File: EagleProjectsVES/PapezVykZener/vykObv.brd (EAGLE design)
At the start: 160 x 100 mm, 19 parts, among them P1 VCC, P2 GND, P3 B, P4 C, P5 E, P6 X4, P7 X3

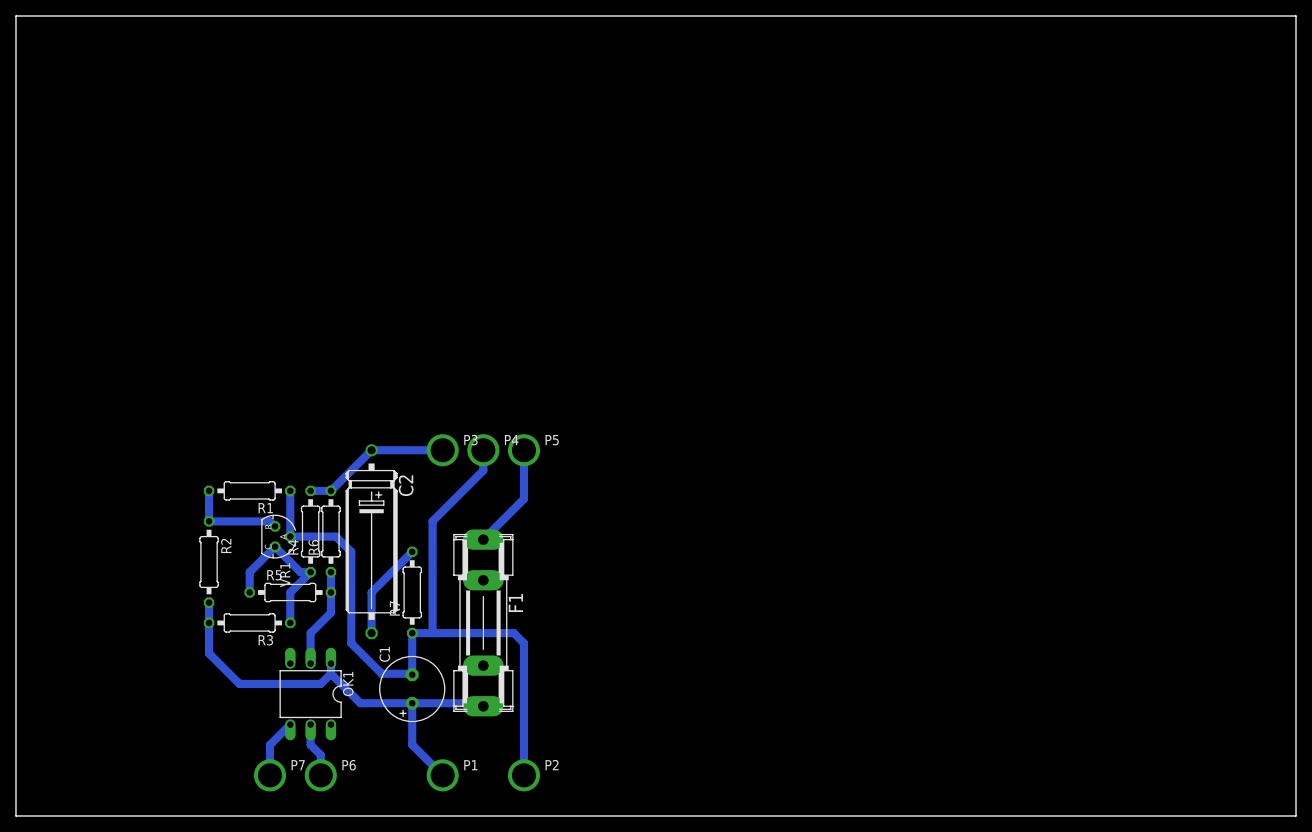
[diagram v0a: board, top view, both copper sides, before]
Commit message: Hotovy vykonovy obvod simulujici zenerovu doidu
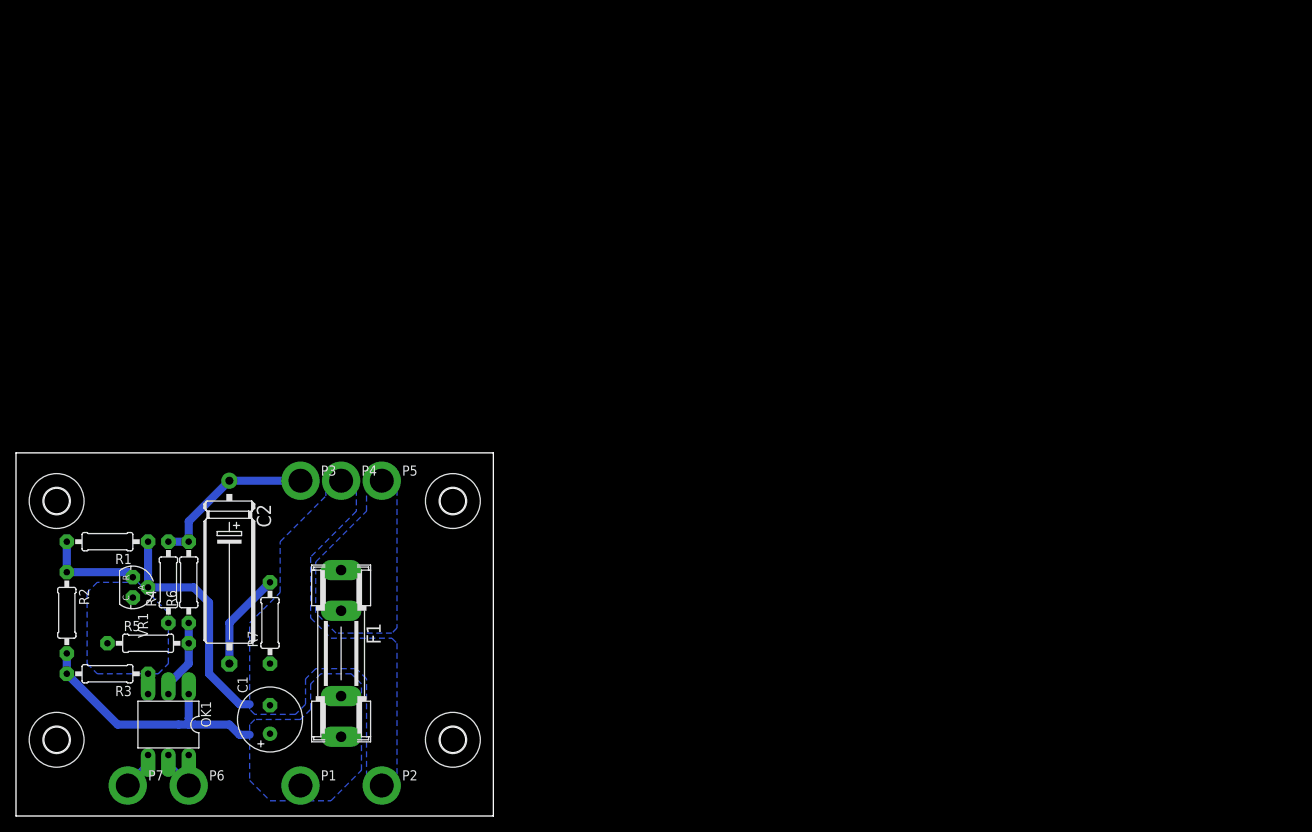
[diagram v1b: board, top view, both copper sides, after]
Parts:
- added U$1, U$2, U$3, U$4: (no value), holes:3,2
- moved R1 18.9 mm to (11.4, 34.3)
- moved R2 18.9 mm to (6.35, 25.4)
- moved R3 18.9 mm to (11.4, 17.8)
- moved R4 18.9 mm to (19.1, 29.2)
- moved R5 18.9 mm to (16.5, 21.6)
- moved R6 18.9 mm to (21.6, 29.2)
- moved VR1 18.9 mm to (14.6, 28.6)
- moved C1 18.2 mm to (31.8, 12.1)
- moved C2 18.2 mm to (26.7, 30.5)
- moved F1 18.2 mm to (40.6, 20.3)
- moved P3 18.2 mm to (35.6, 41.9)
- moved P4 18.2 mm to (40.6, 41.9)
- moved P5 18.2 mm to (45.7, 41.9)
- moved R7 18.2 mm to (31.8, 24.1)
- moved OK1 18.2 mm to (19.1, 11.4)
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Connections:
- net N$2 renamed GND
- removed net N$1: C1.+, F1.2A, OK1.1, P1.1, R2.2, R3.2
- removed net N$3: F1.1A, P5.1
- new net EMIT: F1.1A, F1.1B, P5.1
- new net VDD: C1.+, F1.2A, F1.2B, OK1.1, P1.1, R2.2, R3.2
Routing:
- net GND: track 96.5 -> 29.9 mm
- net N$1: track 56.3 -> 0.00 mm
- net VDD: track 0.00 -> 32.4 mm
- net N$7: track 20.2 -> 0.00 mm
- net N$3: track 13.3 -> 0.00 mm
- net N$5: track 12.5 -> 9.94 mm
- net N$8: track 7.40 -> 4.86 mm
- net N$6: track 18.6 -> 21.2 mm
- net N$9: track 6.88 -> 4.86 mm
- added copper zone on layer 16, net EMIT
- added copper zone on layer 16, net GND
- added copper zone on layer 16, net N$7
- added copper zone on layer 16, net VDD
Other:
- board size 160 x 100 mm -> 59.7 x 45.4 mm

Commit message: Zacatek prace na prednasce P7 pro anglicany
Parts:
- P6, P7: device PADs:PAD3MM -> PADs:PAD1.6MM
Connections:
- net N$8: now also P7.P$1; no longer P7.1
- net N$9: now also P6.P$1; no longer P6.1
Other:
- board text added: "B"
- board text added: "C"
- board text added: "E"
- board text added: "GND"
- board text added: "spodní vrstva"
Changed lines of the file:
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@@
 <grid distance="0.05" unitdist="inch" unit="inch" style="lines" multiple="1" display="yes" altdistance="0.025" altunitdist="inch" altunit="inch"/>
 <layers>
-<layer number="1" name="Top" color="4" fill="1" visible="yes" active="yes"/>
+<layer number="1" name="Top" color="4" fill="1" visible="no" active="yes"/>
 <layer number="2" name="Route2" color="1" fill="3" visible="no" active="no"/>
 <layer number="3" name="Route3" color="4" fill="3" visible="no" active="no"/>
@@
 <layer number="17" name="Pads" color="2" fill="1" visible="yes" active="yes"/>
 <layer number="18" name="Vias" color="2" fill="1" visible="yes" active="yes"/>
-<layer number="19" name="Unrouted" color="6" fill="1" visible="yes" active="yes"/>
+<layer number="19" name="Unrouted" color="6" fill="1" visible="no" active="yes"/>
 <layer number="20" name="Dimension" color="15" fill="1" visible="yes" active="yes"/>
-<layer number="21" name="tPlace" color="7" fill="1" visible="yes" active="yes"/>
-<layer number="22" name="bPlace" color="7" fill="1" visible="yes" active="yes"/>
-<layer number="23" name="tOrigins" color="15" fill="1" visible="yes" active="yes"/>
-<layer number="24" name="bOrigins" color="15" fill="1" visible="yes" active="yes"/>
-<layer number="25" name="tNames" color="7" fill="1" visible="yes" active="yes"/>
-<layer number="26" name="bNames" color="7" fill="1" visible="yes" active="yes"/>
-<layer number="27" name="tValues" color="7" fill="1" visible="yes" active="yes"/>
-<layer number="28" name="bValues" color="7" fill="1" visible="yes" active="yes"/>
+<layer number="21" name="tPlace" color="7" fill="1" visible="no" active="yes"/>
+<layer number="22" name="bPlace" color="7" fill="1" visible="no" active="yes"/>
+<layer number="23" name="tOrigins" color="15" fill="1" visible="no" active="yes"/>
+<layer number="24" name="bOrigins" color="15" fill="1" visible="no" active="yes"/>
+<layer number="25" name="tNames" color="7" fill="1" visible="no" active="yes"/>
+<layer number="26" name="bNames" color="7" fill="1" visible="no" active="yes"/>
+<layer number="27" name="tValues" color="7" fill="1" visible="no" active="yes"/>
+<layer number="28" name="bValues" color="7" fill="1" visible="no" active="yes"/>
 <layer number="29" name="tStop" color="7" fill="3" visible="no" active="yes"/>
 <layer number="30" name="bStop" color="7" fill="6" visible="no" active="yes"/>
@@
 <layer number="37" name="tTest" color="7" fill="1" visible="no" active="yes"/>
 <layer number="38" name="bTest" color="7" fill="1" visible="no" active="yes"/>
-<layer number="39" name="tKeepout" color="4" fill="11" visible="yes" active="yes"/>
-<layer number="40" name="bKeepout" color="1" fill="11" visible="yes" active="yes"/>
-<layer number="41" name="tRestrict" color="4" fill="10" visible="yes" active="yes"/>
-<layer number="42" name="bRestrict" color="1" fill="10" visible="yes" active="yes"/>
-<layer number="43" name="vRestrict" color="2" fill="10" visible="yes" active="yes"/>
+<layer number="39" name="tKeepout" color="4" fill="11" visible="no" active="yes"/>
+<layer number="40" name="bKeepout" color="1" fill="11" visible="no" active="yes"/>
+<layer number="41" name="tRestrict" color="4" fill="10" visible="no" active="yes"/>
+<layer number="42" name="bRestrict" color="1" fill="10" visible="no" active="yes"/>
+<layer number="43" name="vRestrict" color="2" fill="10" visible="no" active="yes"/>
 <layer number="44" name="Drills" color="7" fill="1" visible="no" active="yes"/>
 <layer number="45" name="Holes" color="7" fill="1" visible="no" active="yes"/>
 <layer number="46" name="Milling" color="3" fill="1" visible="no" active="yes"/>
 <layer number="47" name="Measures" color="7" fill="1" visible="no" active="yes"/>
-<layer number="48" name="Document" color="7" fill="1" visible="yes" active="yes"/>
-<layer number="49" name="Reference" color="7" fill="1" visible="yes" active="yes"/>
-<layer number="51" name="tDocu" color="7" fill="1" visible="yes" active="yes"/>
-<layer number="52" name="bDocu" color="7" fill="1" visible="yes" active="yes"/>
+<layer number="48" name="Document" color="7" fill="1" visible="no" active="yes"/>
+<layer number="49" name="Reference" color="7" fill="1" visible="no" active="yes"/>
+<layer number="51" name="tDocu" color="7" fill="1" visible="no" active="yes"/>
+<layer number="52" name="bDocu" color="7" fill="1" visible="no" active="yes"/>
 <layer number="90" name="Modules" color="5" fill="1" visible="no" active="no"/>
 <layer number="91" name="Nets" color="2" fill="1" visible="no" active="no"/>
@@
 <dimension x1="5.08" y1="39.37" x2="54.61" y2="39.37" x3="29.845" y3="49.53" textsize="1.778" layer="51"/>
 <dimension x1="5.08" y1="9.525" x2="5.08" y2="39.37" x3="-5.08" y3="24.4475" textsize="1.778" layer="51"/>
+<text x="50.8" y="15.24" size="2.1844" layer="16" rot="MR90">spodní vrstva</text>
+<text x="50.8" y="38.1" size="2.1844" layer="16" rot="MR0">E</text>
+<text x="32.385" y="38.1" size="2.1844" layer="16" rot="MR0">B</text>
+<text x="55.88" y="2.54" size="2.1844" layer="16" rot="MR0">GND</text>
+<text x="12.7" y="5.08" size="2.1844" layer="16" rot="MR0">C</text>
+<text x="25.4" y="5.08" size="2.1844" layer="16" rot="MR0">E</text>
 </plain>
 <attributes>
@@
 <attribute name="DIAMETER" value="3mm" x="45.72" y="41.91" size="1.778" layer="27" display="off"/>
 </element>
-<element name="P6" library="PADs" package="PAD3MM" value="X4" x="21.59" y="3.81">
-<attribute name="DIAMETER" value="3mm" x="21.59" y="3.81" size="1.778" layer="27" display="off"/>
-</element>
-<element name="P7" library="PADs" package="PAD3MM" value="X3" x="13.97" y="3.81">
-<attribute name="DIAMETER" value="3mm" x="13.97" y="3.81" size="1.778" layer="27" display="off"/>
-</element>
+<element name="P6" library="PADs" package="PAD1.6MM" value="X4" x="21.59" y="3.81"/>
+<element name="P7" library="PADs" package="PAD1.6MM" value="X3" x="13.97" y="3.81"/>
 <element name="R1" library="rcl" package="0207/10" value="2k2" x="11.43" y="34.29" rot="R180"/>
 <element name="R2" library="rcl" package="0207/10" value="1k27" x="6.35" y="25.4" rot="R270"/>
@@
 <vertex x="17.78" y="17.78"/>
 <vertex x="19.05" y="19.05"/>
-<vertex x="19.05" y="25.4"/>
-<vertex x="15.24" y="29.21"/>
+<vertex x="19.05" y="26.67"/>
+<vertex x="16.51" y="29.21"/>
 <vertex x="10.16" y="29.21"/>
 <vertex x="8.89" y="27.94"/>
@@
 <signal name="N$8">
 <contactref element="OK1" pad="4"/>
-<contactref element="P7" pad="1"/>
+<contactref element="P7" pad="P$1"/>
 <wire x1="16.51" y1="7.62" x2="16.51" y2="6.35" width="1.016" layer="16"/>
 <wire x1="16.51" y1="6.35" x2="13.97" y2="3.81" width="1.016" layer="16"/>
@@
 <signal name="N$9">
 <contactref element="OK1" pad="5"/>
-<contactref element="P6" pad="1"/>
+<contactref element="P6" pad="P$1"/>
 <wire x1="19.05" y1="7.62" x2="19.05" y2="6.35" width="1.016" layer="16"/>
 <wire x1="19.05" y1="6.35" x2="21.59" y2="3.81" width="1.016" layer="16"/>

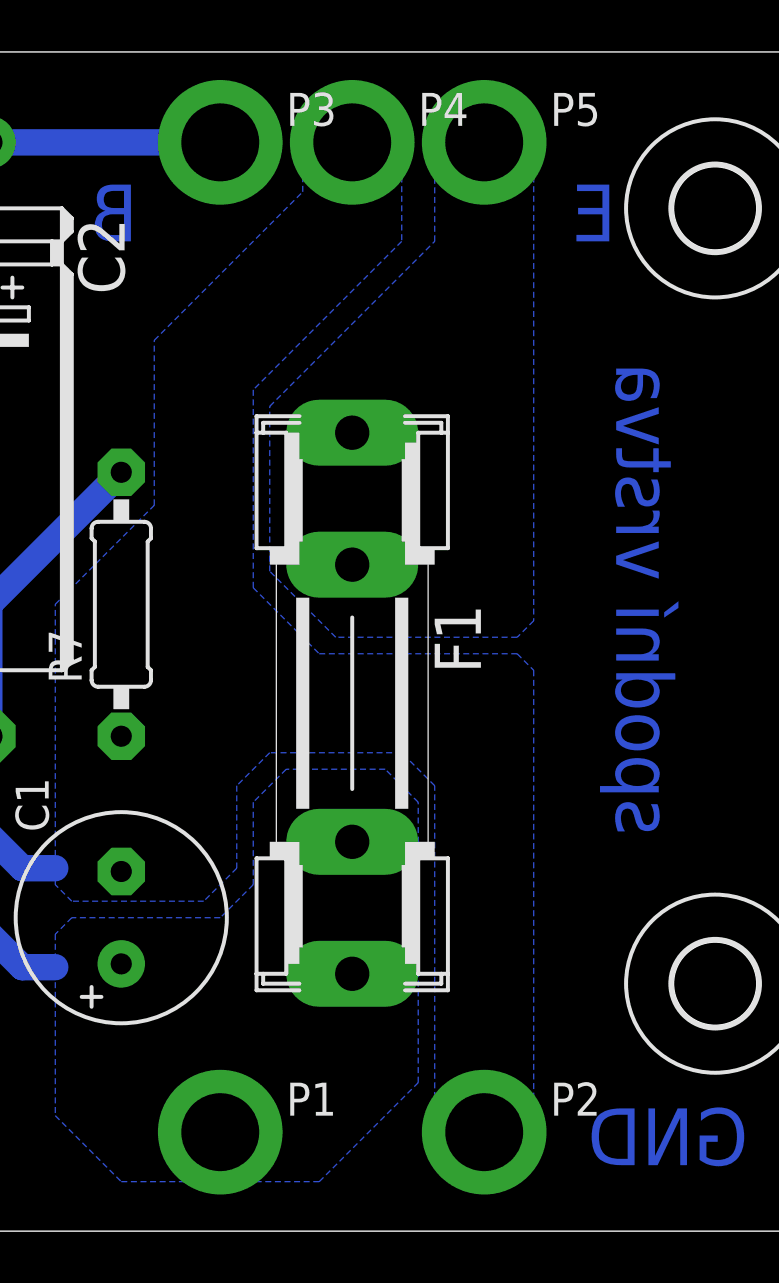
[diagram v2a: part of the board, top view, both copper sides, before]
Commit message: Hotovy panel pro Papezovu zenerku - zmensene prumery padu
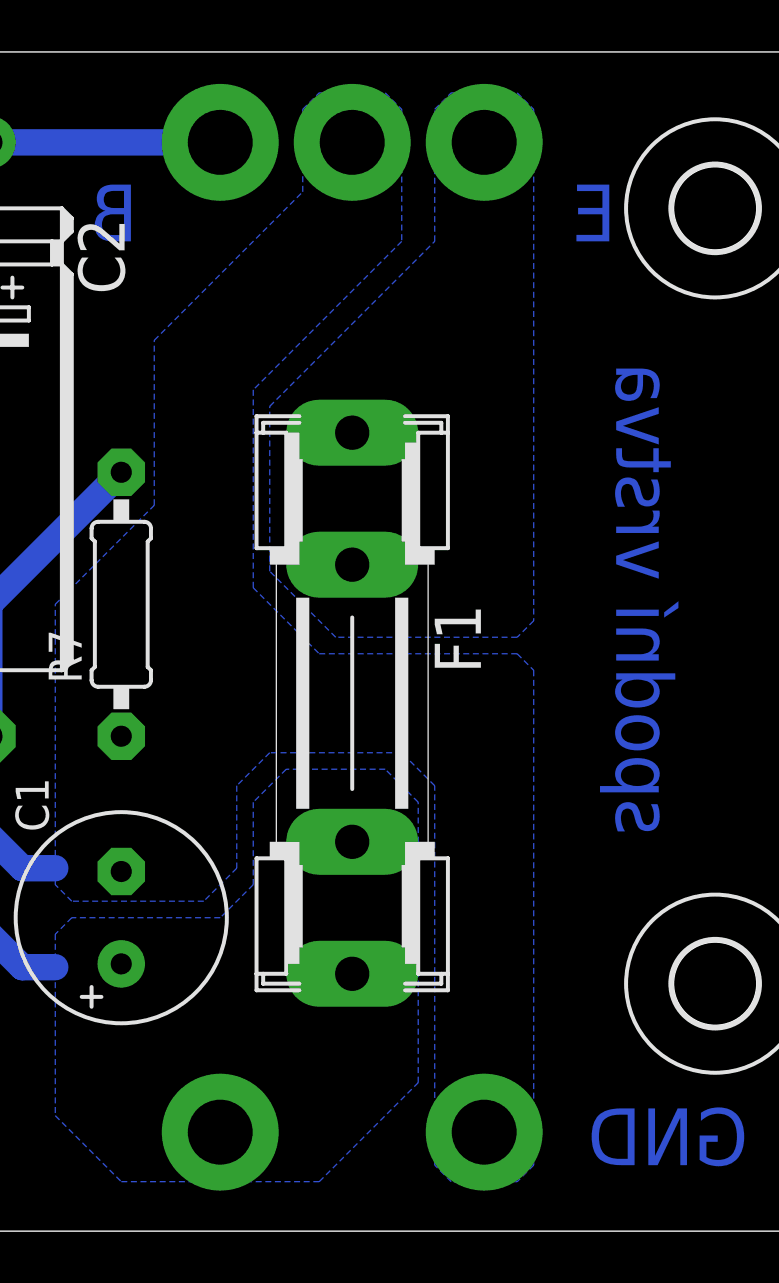
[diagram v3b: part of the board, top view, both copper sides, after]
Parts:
- P1, P2, P3, P4, P5: device PADs:PAD3MM -> PADs:PAD2.5MM
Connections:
- net EMIT: now also P5.P$1; no longer P5.1
- net GND: now also P2.P$1, P4.P$1; no longer P2.1, P4.1
- net N$6: now also P3.P$1; no longer P3.1
- net VDD: now also P1.P$1; no longer P1.1
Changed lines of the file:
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@@
 <attribute name="OC_FARNELL" value="1328375" x="19.05" y="11.43" size="1.778" layer="27" rot="R180" display="off"/>
 </element>
-<element name="P1" library="PADs" package="PAD3MM" value="VCC" x="35.56" y="3.81">
-<attribute name="DIAMETER" value="3mm" x="35.56" y="3.81" size="1.778" layer="27" display="off"/>
-</element>
-<element name="P2" library="PADs" package="PAD3MM" value="GND" x="45.72" y="3.81">
-<attribute name="DIAMETER" value="3mm" x="45.72" y="3.81" size="1.778" layer="27" display="off"/>
-</element>
-<element name="P3" library="PADs" package="PAD3MM" value="B" x="35.56" y="41.91">
-<attribute name="DIAMETER" value="3mm" x="35.56" y="41.91" size="1.778" layer="27" display="off"/>
-</element>
-<element name="P4" library="PADs" package="PAD3MM" value="C" x="40.64" y="41.91">
-<attribute name="DIAMETER" value="3mm" x="40.64" y="41.91" size="1.778" layer="27" display="off"/>
-</element>
-<element name="P5" library="PADs" package="PAD3MM" value="E" x="45.72" y="41.91">
-<attribute name="DIAMETER" value="3mm" x="45.72" y="41.91" size="1.778" layer="27" display="off"/>
-</element>
+<element name="P1" library="PADs" package="PAD2.5MM" value="VCC" x="35.56" y="3.81"/>
+<element name="P2" library="PADs" package="PAD2.5MM" value="GND" x="45.72" y="3.81"/>
+<element name="P3" library="PADs" package="PAD2.5MM" value="B" x="35.56" y="41.91"/>
+<element name="P4" library="PADs" package="PAD2.5MM" value="C" x="40.64" y="41.91"/>
+<element name="P5" library="PADs" package="PAD2.5MM" value="E" x="45.72" y="41.91"/>
 <element name="P6" library="PADs" package="PAD1.6MM" value="X4" x="21.59" y="3.81"/>
 <element name="P7" library="PADs" package="PAD1.6MM" value="X3" x="13.97" y="3.81"/>
@@
 <signals>
 <signal name="VDD">
-<contactref element="P1" pad="1"/>
+<contactref element="P1" pad="P$1"/>
 <contactref element="C1" pad="+"/>
 <contactref element="F1" pad="2A"/>
@@
 <signal name="GND">
 <contactref element="C1" pad="-"/>
-<contactref element="P2" pad="1"/>
-<contactref element="P4" pad="1"/>
+<contactref element="P2" pad="P$1"/>
+<contactref element="P4" pad="P$1"/>
 <contactref element="R1" pad="1"/>
 <contactref element="VR1" pad="A"/>
@@
 <signal name="EMIT">
 <contactref element="F1" pad="1A"/>
-<contactref element="P5" pad="1"/>
+<contactref element="P5" pad="P$1"/>
 <polygon width="0.6096" layer="16" rank="2">
 <vertex x="37.465" y="25.4"/>
@@
 <signal name="N$6">
 <contactref element="R6" pad="2"/>
-<contactref element="P3" pad="1"/>
+<contactref element="P3" pad="P$1"/>
 <contactref element="C2" pad="+"/>
 <contactref element="R4" pad="2"/>
